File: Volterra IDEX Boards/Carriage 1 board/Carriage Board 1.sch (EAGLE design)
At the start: 28 parts, among them K1 FFC/FPC/34PIN/1MMPITCH/TOPLOCK, K2 FFC/FPC/34PIN/1MMPITCH/TOPLOCK, K3 FFC/FPC/34PIN/1MMPITCH/TOPLOCK

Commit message: Switching of carriage board numbering, changing extruder FFC pins and fixing routings
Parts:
- removed K3: FFC/FPC/34PIN/1MMPITCH/TOPLOCK, FracktalWorks_Eagle_Library:FFC/FPC/34PIN/1MMPITCH/TOPLOCK
- removed TP14, TP15, TP16, TP17, TP18, TP19, TP2, TP20, TP21, TP22: TEST-POINTTP_15TH_THRU, SparkFun-Connectors:TEST-POINTTP_15TH_THRU
- removed U$1: FWLOGO, FracktalWorks_Eagle_Library:FWLOGO
- added X1: EXTDR-0, Rembrandt Electronics - JST XH Connectors v1-0:JST-XH-04-PIN-LONG-PAD
- added X4: 24V, Rembrandt Electronics - JST XH Connectors v1-0:JST-XH-02-PIN-LONG-PAD
- added X5: X_LMT, Rembrandt Electronics - JST XH Connectors v1-0:JST-XH-02-PIN-LONG-PAD
- FRAME1: value FRAME-LETTER -> FRAME-LEDGER; device SparkFun-Aesthetics:FRAME-LETTER -> SparkFun-Aesthetics:FRAME-LEDGER
- K2: value FFC/FPC/34PIN/1MMPITCH/TOPLOCK -> Tool 0; device FracktalWorks_Eagle_Library:FFC/FPC/34PIN/1MMPITCH/TOPLOCK -> Wurth_Elektronik_Electromechanic_FPC_Connectors_&_Flat_Flexible_Cable_rev15b:68611214122
- U$2: value FRACKTALLOGO -> FWLOGO; device FracktalWorks_Eagle_Library:FRACKTALLOGO -> FracktalWorks_Eagle_Library:FWLOGO
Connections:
- removed net A0+: K1.27, K2.26, K2.27, TP20.1
- removed net A0-: K1.28, K2.24, K2.25, TP9.1
- removed net B0+: K1.29, K2.30, K2.31, TP19.1
- removed net B0-: K1.30, K2.28, K2.29, TP18.1
- removed net H0+: K1.1, K1.2, K1.3, K1.4, K2.2, K2.3, K2.4, K2.5, K2.6, TP21.1
- removed net H0-: K1.5, K1.6, K1.7, K1.8, K2.10, K2.11, K2.12, K2.8, K2.9, TP1.1
- removed net PT0: K1.9, K2.14, TP2.1
- removed net X2_LMT: K1.23, K3.17, TP12.1
- removed net Y_LMT: K1.21, TP13.1
- net 24V: now also K1.21, K2.2, TP1.1, X4-1.S; no longer K1.25, K2.21, K3.14, TP7.1
- net 5V: now also K1.22; no longer K1.26, K2.22, K3.13, TP8.1
- net A1+: now also K1.26, K1.27, TP10.1, X1-1.S; no longer K1.31, K3.8, K3.9, TP15.1
- net A1-: now also K1.24, K1.25, TP11.1, X1-2.S; no longer K1.32, K3.10, K3.11, TP14.1
- net B1+: now also K1.30, K1.31, TP12.1, X1-3.S; no longer K1.33, K3.4, K3.5, TP17.1
- net B1-: now also K1.28, K1.29, TP13.1, X1-4.S; no longer K1.34, K3.6, K3.7, TP16.1
- net CF+: now also K1.15, K2.5, TP6.1; no longer K1.11, K2.15, K3.20, TP3.1
- net CF-: now also K1.16, K2.4, TP7.1; no longer K1.10, K2.16, K3.19, TP4.1
- net GND: now also K1.19, K2.1, TP3.1, X4-2.S, X5-2.S; no longer K1.24, K2.19, K3.16, TP6.1
- net H1+: now also K1.2, K1.3, K1.4, K1.5, K1.6, K2.10, K2.11, K2.12, TP8.1; no longer K1.12, K1.13, K1.14, K1.15, K3.29, K3.30, K3.31, K3.32, K3.33, TP22.1
- net H1-: now also K1.10, K1.11, K1.12, K1.8, K1.9, K2.7, K2.8, K2.9, TP9.1; no longer K1.16, K1.17, K1.18, K1.19, K3.23, K3.24, K3.25, K3.26, K3.27, TP10.1
- net PT1: now also K1.14, K2.6, TP4.1; no longer K1.20, K3.21, TP11.1
- net X1_LMT: now also K1.18, X5-1.S; no longer K1.22, K2.18
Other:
- note added: "C:/Users/Vijay/Dropbox/FracktalWorks/Design & Marketing Colaterals/Box Logo.bmp"
- moved on the sheet: K1, TP1, TP10, TP11, TP12, TP13, TP3, TP4, TP5, TP6, TP7, TP8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

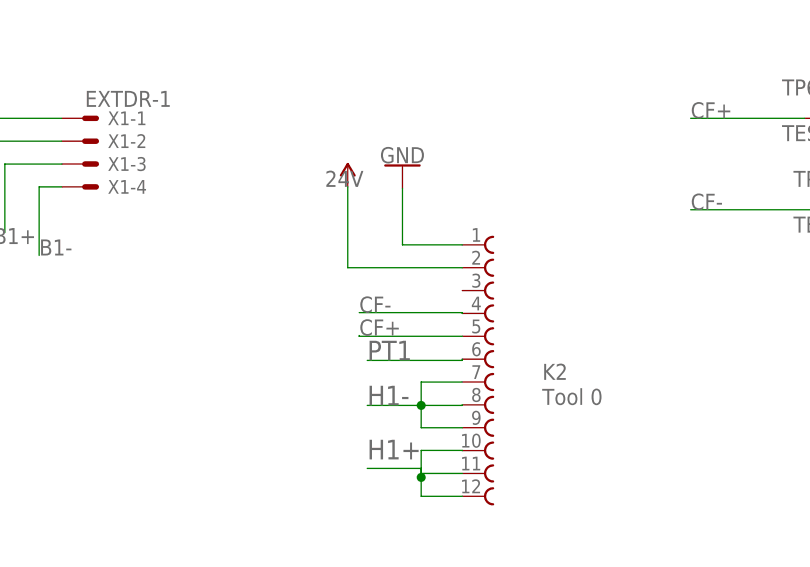
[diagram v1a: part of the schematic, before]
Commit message: Updated Daughter board schematic and other boards
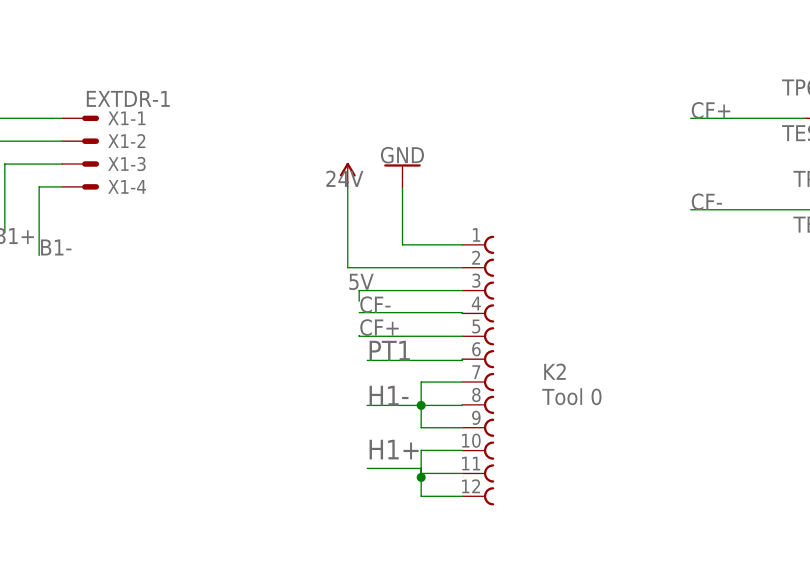
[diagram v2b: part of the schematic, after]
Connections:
- net 5V: now also K2.3
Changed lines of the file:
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@@
 <label x="-387.35" y="116.84" size="1.778" layer="95"/>
+</segment>
+<segment>
+<pinref part="K2" gate="G$1" pin="3"/>
+<wire x1="-300.97" y1="92.62" x2="-312.42" y2="92.62" width="0.1524" layer="91"/>
+<wire x1="-312.42" y1="92.62" x2="-312.42" y2="91.44" width="0.1524" layer="91"/>
+<label x="-313.69" y="92.71" size="1.778" layer="95"/>
 </segment>
 </net>
